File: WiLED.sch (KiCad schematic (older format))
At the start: 46 parts, among them P1 Serial to USB, P2 DC In, P3 Lamp Connector, P4 LED Out, SW1 Reset, SW2 Boot, SW3 Toggle, SW4 Rotary Encoder, U1 ESP-WROOM-32, U2 VXO7803-500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

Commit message: First draft of v2.0 schematic and PCB
This is the first complete schematic and PCB layout for version 2.0 of
the WiLED main board. Some tweaks may be needed, but the general concept
is complete.
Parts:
- added D7: 1SS404, Diodes_SMD:D_SOD-323, symbol D_Schottky
- added R16: 1k, Resistors_SMD:R_0805_HandSoldering, symbol R
- added R17, R18: 10k, Resistors_SMD:R_0603, symbol R
- C1, C10, C11, C12, C2, C3, C4, C5, C7, C8, C9: footprint Capacitors_SMD:C_0805_HandSoldering -> Capacitors_SMD:C_0805
- C6: footprint Capacitors_SMD:C_1812_HandSoldering -> Capacitors_SMD:C_1812
- D1, D3, D4, D5: footprint LEDs:LED-3MM -> custom-footprints:WL-SMCW
- D2: footprint LEDs:LED-3MM -> LEDs:LED_D3.0mm
- D6: footprint (none) -> Diodes_SMD:D_SOD-123
- L1: value 12uH -> 12 uH; footprint custom-footprints:THT_Inductor_small -> custom-footprints:THT_Inductor_5mm
- L2: footprint custom-footprints:THT_Inductor_small -> custom-footprints:THT_Inductor_5mm
- P1: footprint Pin_Headers:Pin_Header_Straight_1x06 -> Pin_Headers:Pin_Header_Straight_1x06_Pitch2.54mm
- P2, P4: footprint Connectors_JST:JST_PH_B2B-PH-K_02x2.00mm_Straight -> custom-footprints:Terminal
- R1, R10, R11, R12, R13, R14, R15, R4, R5, R6, R7, R8, R9: footprint Resistors_SMD:R_0805_HandSoldering -> Resistors_SMD:R_0603
- R2, R3: value 4.7k -> 10k; footprint Resistors_SMD:R_0805_HandSoldering -> Resistors_SMD:R_0603
- SW1, SW2: footprint (none) -> custom-footprints:Button_6.5mm
- SW3: footprint (none) -> Pin_Headers:Pin_Header_Straight_1x03_Pitch2.00mm
- SW4: footprint (none) -> custom-footprints:PEC11R_5
- U2: footprint custom-footprints:Recom_R-78HBxx-0.5 -> custom-footprints:VXO78-500
- U3: footprint (none) -> TO_SOT_Packages_SMD:SOT-23-5_HandSoldering
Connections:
- net +3V3: now also D7.1 (K)
- net ENC_A: now also R18.2; no longer P3.3 (P3), R10.2, SW4.1 (A)
- net ENC_B: now also R17.2; no longer P3.4 (P4), R11.2, SW4.3 (B)
- net GND: now also U1.39 (GND_PAD), R16.2
- net at P1.3 (P3): now also D7.2 (A)
- net at U1.23 (IO15): now also R16.1
- new net CON_A: P3.3 (P3), R10.2, R18.1, SW4.1 (A)
- new net CON_B: P3.4 (P4), R11.2, R17.1, SW4.3 (B)
- no-connect marks 23 -> 20
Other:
- note added: "C4 is optional"
- note added: "R16 is optional"
- note removed: "Encoder Biasing"
- moved on the sheet: C10, C11, C7, C8, C9, P1, R10, R11, R12, R13, R9, SW3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

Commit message: Rework LED constant-current PCB layout
Previously there were unnecssarily long traces between high-power
components in the buck-mode LED driver, this commit brings a modified
layout that tries to improve on this.
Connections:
- net LED_NEG: now also P4.2; no longer P4.1
- net LED_POS: now also P4.1; no longer P4.2
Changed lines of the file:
@@
 Sheet 1 1
 Title "WiLED ESP32 Base"
-Date "2018-07-01"
+Date "2018-07-02"
 Rev "2.0"
 Comp "Sean Lanigan"
@@
 F 3 "" H 9925 4300 50  0001 C CNN
 	1    9950 4300
-	1    0    0    1
-$EndComp
-$Comp
+	1    0    0    -1
+$EndComp
+$Comp

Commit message: Add PIR sensor and more stitching vias
Added a connection for a HC-SR501 PIR sensor, to a spare GPIO on the
ESP-32.
Also increased the number of stitching vias.
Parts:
- added U4: HC-SR501, Pin_Headers:Pin_Header_Straight_1x03_Pitch2.00mm, symbol HC-SR501
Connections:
- net +3V3: now also U4.3 (Vcc)
- net GND: now also U4.1 (GND)
- net PIR_TRG: now reaches U1.27 (IO16)
- net PIR_TRG: now also U4.2 (Out)
- no-connect marks 20 -> 19
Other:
- note added: "Passive Infrared Sensor"
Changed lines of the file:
@@
 Sheet 1 1
 Title "WiLED ESP32 Base"
-Date "2018-07-02"
+Date "2018-07-08"
 Rev "2.0"
 Comp "Sean Lanigan"
@@
 	7450 5950 7450 6000
 Connection ~ 7450 5950
-NoConn ~ 4000 3000
 NoConn ~ 4000 2900
 NoConn ~ 4000 2800
@@
 Text Notes 2700 4700 0    50   ~ 0
 R16 is optional
+$Comp
+L HC-SR501 U4
+U 1 1 5B4045C3
+P 6400 7050
+F 0 "U4" H 6550 7350 60  0000 C CNN
+F 1 "HC-SR501" H 6400 6750 60  0000 C CNN
+F 2 "Pin_Headers:Pin_Header_Straight_1x03_Pitch2.00mm" H 6400 6950 60  0001 C CNN
+F 3 "" H 6400 6950 60  0001 C CNN
+	1    6400 7050
+	1    0    0    -1
+$EndComp
+Wire Notes Line
+	5150 6500 6800 6500
+Wire Notes Line
+	6800 6500 6800 7650
+Wire Notes Line
+	6800 7650 5150 7650
+Wire Notes Line
+	5150 7650 5150 6500
+$Comp
+L +3.3V #PWR028
+U 1 1 5B40519F
+P 5450 6800
+F 0 "#PWR028" H 5450 6650 50  0001 C CNN
+F 1 "+3.3V" H 5450 6940 50  0000 C CNN
+F 2 "" H 5450 6800 50  0000 C CNN
+F 3 "" H 5450 6800 50  0000 C CNN
+	1    5450 6800
+	1    0    0    -1
+$EndComp
+$Comp
+L GND #PWR029
+U 1 1 5B405342
+P 5450 7300
+F 0 "#PWR029" H 5450 7050 50  0001 C CNN
+F 1 "GND" H 5450 7150 50  0000 C CNN
+F 2 "" H 5450 7300 50  0000 C CNN
+F 3 "" H 5450 7300 50  0000 C CNN
+	1    5450 7300
+	1    0    0    -1
+$EndComp
+Wire Wire Line
+	5450 6800 5450 6900
+Wire Wire Line
+	5450 6900 6000 6900
+Wire Wire Line
+	5450 7300 5450 7200
+Wire Wire Line
+	5450 7200 6000 7200
+Text GLabel 5900 7050 0    60   3State ~ 0
+PIR_TRG
+Wire Wire Line
+	5900 7050 6000 7050
+Text GLabel 4150 3000 2    47   3State ~ 0
+PIR_TRG
+Wire Wire Line
+	4000 3000 4150 3000
+Text Notes 5250 6450 0    60   ~ 0
+Passive Infrared Sensor
 $EndSCHEMATC

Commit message: Correct pin mappings from unusable ESP32 pins
Some LED indicators were assigned to ESP32 pins which are only available
for input, and the toggle switch was mapped to the MTDO pin. Both of
these mistakes are corrected in this commit.
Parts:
- C1, C10, C11, C2, C3, C4, C7, C8, C9: footprint Capacitors_SMD:C_0805 -> Capacitor_SMD:C_0805_2012Metric; symbol C -> WiLED-rescue:C
- C12, C5: footprint Capacitors_SMD:C_0805 -> Capacitor_SMD:C_1206_3216Metric; symbol C -> WiLED-rescue:C
- C6: footprint Capacitors_SMD:C_1812 -> Capacitor_SMD:C_1206_3216Metric; symbol C -> WiLED-rescue:C
- D1, D2, D3, D4, D5: symbol LED_ALT -> WiLED-rescue:LED_ALT
- D6, D7: symbol D_Schottky -> WiLED-rescue:D_Schottky
- L1, L2: symbol L -> WiLED-rescue:L
- P1: symbol CONN_01X06 -> WiLED-rescue:CONN_01X06
- P2, P4: symbol Screw_Terminal_1x02 -> WiLED-rescue:Screw_Terminal_1x02
- P3: symbol CONN_01X07 -> WiLED-rescue:CONN_01X07
- R1, R10, R11, R15, R17, R18, R2, R3, R9: footprint Resistors_SMD:R_0603 -> Resistor_SMD:R_0603_1608Metric; symbol R -> WiLED-rescue:R
- R12, R13: value 10k -> DNF; footprint Resistors_SMD:R_0603 -> Resistor_SMD:R_0603_1608Metric; symbol R -> WiLED-rescue:R
- R14: footprint Resistors_SMD:R_0603 -> Resistor_SMD:R_0805_2012Metric; symbol R -> WiLED-rescue:R
- R16: footprint Resistors_SMD:R_0805_HandSoldering -> Resistor_SMD:R_0805_2012Metric_Pad1.15x1.40mm_HandSolder; symbol R -> WiLED-rescue:R
- R4, R5, R7: value 680 -> 330; footprint Resistors_SMD:R_0603 -> Resistor_SMD:R_0603_1608Metric; symbol R -> WiLED-rescue:R
- R6, R8: value 680 -> 1k; footprint Resistors_SMD:R_0603 -> Resistor_SMD:R_0603_1608Metric; symbol R -> WiLED-rescue:R
- SW1, SW2: symbol SWITCH_SPST -> WiLED-rescue:SWITCH_SPST
- SW3: symbol SWITCH_SPDT -> WiLED-rescue:SWITCH_SPDT
- SW4: symbol Rotary_Encoder_Switch -> WiLED-rescue:Rotary_Encoder_Switch
- U1: symbol ESP32-WROOM -> espressif-xess:ESP32-WROOM
- U2: symbol R-78E-0.5 -> Regulator_Linear:LF33_TO220
- U3: symbol AL8860WT-7 -> WiLED-rescue:AL8860WT-7
- U4: symbol HC-SR501 -> WiLED-rescue:HC-SR501
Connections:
- net TGL_1: now also U1.13 (IO14); no longer U1.14 (IO12)
- net IO17: now reaches U1.28 (IO17)
- net IO17: now also D3.2 (A)
- net IO18: now reaches U1.30 (IO18)
- net IO18: now also D4.2 (A)
- net IO19: now reaches U1.31 (IO19)
- net IO19: now also D5.2 (A)
- net IO33: no longer names the net of U1.9 (IO33)
- net IO33: no longer D3.2 (A)
- net IO34: no longer names the net of U1.6 (IO34)
- net IO34: no longer D4.2 (A)
- net IO35: no longer names the net of U1.7 (IO35)
- net IO35: no longer D5.2 (A)
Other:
- note added: "Do not\nfit R12"
- note added: "Do not\nfit R13"
- moved on the sheet: U2

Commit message: Update PCB for KiCad 5, and begin rerouting for new PSU
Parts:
- removed P3: Lamp Connector, Connectors_JST:JST_PH_B7B-PH-K_07x2.00mm_Straight, symbol WiLED-rescue:CONN_01X07
- removed U2: VXO7803-500, custom-footprints:VXO78-500, symbol Regulator_Linear:LF33_TO220
- added C13: 10uF, Capacitor_SMD:C_1206_3216Metric, symbol Device:C
- added C14: 100nF, Capacitor_SMD:C_0805_2012Metric, symbol Device:C
- added D8: SS14FL, Diode_SMD:D_SOD-123F, symbol Device:D_Schottky
- added J1, J2, J3, J4: Mount, MountingHole:MountingHole_3.2mm_M3_ISO14580_Pad, symbol Connector:Screw_Terminal_01x01
- added U2: TS3004x, Package_DFN_QFN:QFN-16-1EP_3x3mm_P0.5mm_EP2.7x2.7mm_ThermalVias, symbol WiLED-rescue:TS3004x
- C4: value 4.7uF -> 22nF
- C5: value 10uF -> 22uF
- C6: value 100uF -> 22uF
- D2: value Indicator LED -> Ind. LED 1
- D5: value Status 3 LED -> Ind. LED 2
- D6: footprint Diodes_SMD:D_SOD-123 -> Diode_SMD:D_SOD-123F
- D7: footprint Diodes_SMD:D_SOD-323 -> Diode_SMD:D_SOD-323
- L1: value 12 uH -> 4.7uH; footprint custom-footprints:THT_Inductor_5mm -> Inductor_SMD:L_Taiyo-Yuden_NR-40xx
- R12, R13: value DNF -> 10k
- R16: footprint Resistor_SMD:R_0805_2012Metric_Pad1.15x1.40mm_HandSolder -> Resistor_SMD:R_0603_1608Metric_Pad1.05x0.95mm_HandSolder
- U3: footprint TO_SOT_Packages_SMD:SOT-23-5_HandSoldering -> Package_TO_SOT_SMD:SOT-23-5
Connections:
- net +3V3: now also C5.1, L1.2, U2.5 (FB)
- net GND: now also P2.2, C13.2, C14.2, D8.2 (A), J1.1 (Pin_1), J2.1 (Pin_1), J3.1 (Pin_1), J4.1 (Pin_1), U2.14 (PGND), U2.15 (PGND), U2.17 (PAD), U2.4 (GND); no longer C4.2, P2.1
- net IND_PWM: now also D5.2 (A)
- net RAW: now also P2.1, C13.1, C14.1, U2.11 (Vcc), U2.2 (Vcc), U2.3 (Vcc); no longer C4.1, L1.1, P2.2
- net IO19: no longer names the net of U1.31 (IO19)
- net IO19: no longer D5.2 (A)
- new net: C4.1, U2.10 (BST)
- new net: C4.2, D8.1 (K), L1.1, U2.1 (VSW), U2.12 (VSW), U2.13 (VSW), U2.16 (VSW)
- no-connect marks 19 -> 22
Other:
- note removed: "C4 is optional"
- note removed: "Do not\nfit R12"
- note removed: "Do not\nfit R13"
- note removed: "Off-board Connectors"
- moved on the sheet: C4, C5, C6, D2, D3, D4, D5, L1, P2, P4, R5, R6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

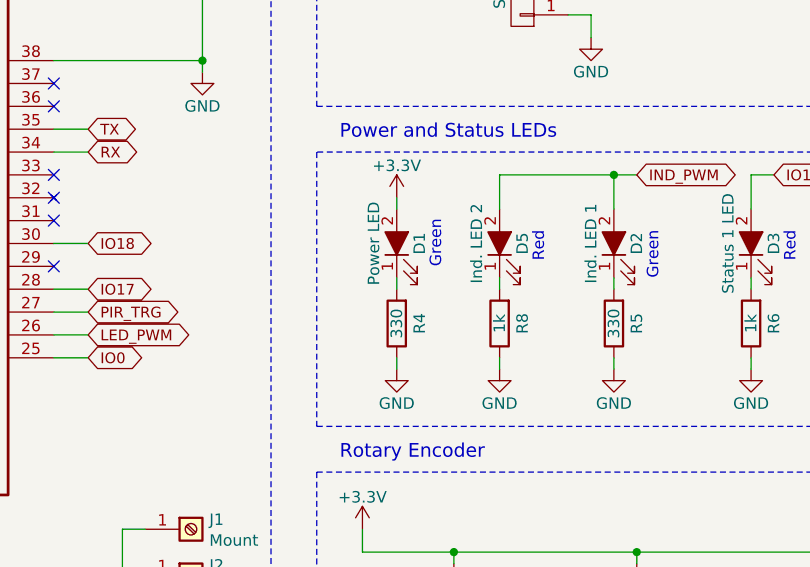
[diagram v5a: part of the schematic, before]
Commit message: Re-designed layout, with less wasted space
Routing is completed, but vias still need to be added. The newer layout
is much more space efficient.
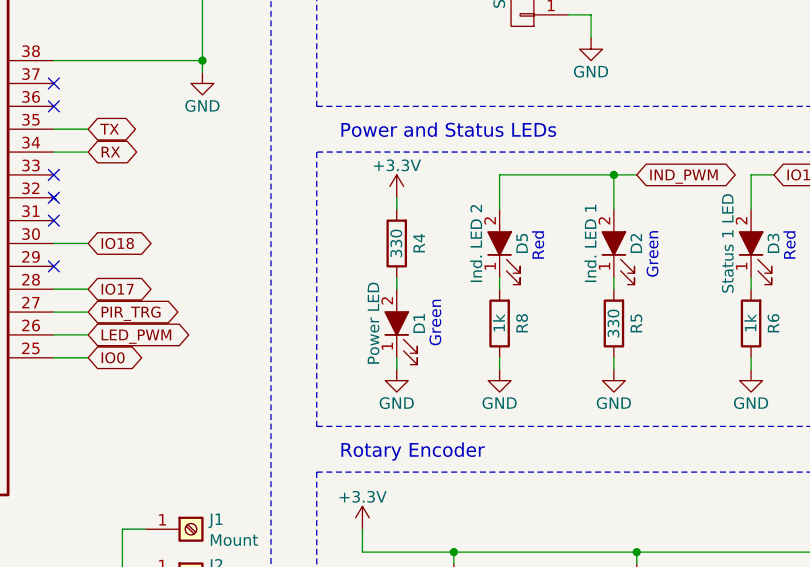
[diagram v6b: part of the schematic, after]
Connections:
- net +3V3: now also R4.2; no longer D1.2 (A)
- net GND: now also D1.1 (K); no longer R4.1
- new net: D1.2 (A), R4.1
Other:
- moved on the sheet: D1, R4
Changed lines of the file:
@@
 L WiLED-rescue:LED_ALT D1
 U 1 1 59B08128
-P 5500 2700
-F 0 "D1" H 5500 2600 50  0000 C CNN
-F 1 "Power LED" H 5500 2800 50  0000 C CNN
-F 2 "custom-footprints:WL-SMCW" H 5500 2700 50  0001 C CNN
-F 3 "" H 5500 2700 50  0000 C CNN
-	1    5500 2700
+P 5500 3050
+F 0 "D1" H 5500 2950 50  0000 C CNN
+F 1 "Power LED" H 5500 3150 50  0000 C CNN
+F 2 "custom-footprints:WL-SMCW" H 5500 3050 50  0001 C CNN
+F 3 "" H 5500 3050 50  0000 C CNN
+	1    5500 3050
 	0    -1   -1   0
 $EndComp
@@
 L WiLED-rescue:R R4
 U 1 1 59B0899F
-P 5500 3050
-F 0 "R4" V 5400 3050 50  0000 C CNN
-F 1 "330" V 5500 3050 50  0000 C CNN
-F 2 "Resistor_SMD:R_0603_1608Metric" V 5430 3050 50  0001 C CNN
-F 3 "" H 5500 3050 50  0000 C CNN
-	1    5500 3050
+P 5500 2700
+F 0 "R4" V 5400 2700 50  0000 C CNN
+F 1 "330" V 5500 2700 50  0000 C CNN
+F 2 "Resistor_SMD:R_0603_1608Metric" V 5430 2700 50  0001 C CNN
+F 3 "" H 5500 2700 50  0000 C CNN
+	1    5500 2700
 	-1   0    0    1
 $EndComp
-Text Notes 5700 2600 3    50   ~ 0
+Text Notes 5700 2950 3    50   ~ 0
 Green
 Text GLabel 7300 4450 0    47   BiDi ~ 0
